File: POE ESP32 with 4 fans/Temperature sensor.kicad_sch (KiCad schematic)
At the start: 1 part, among them U1 DS18B20

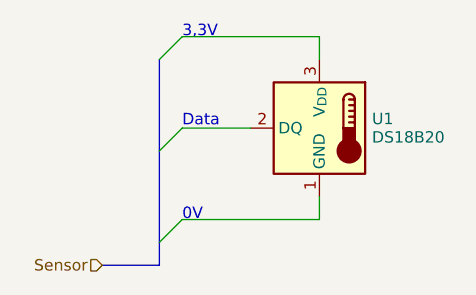
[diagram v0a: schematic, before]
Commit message: Assigned footprints to multiple symbols Removed automatic workflow triggering. Will change in the future
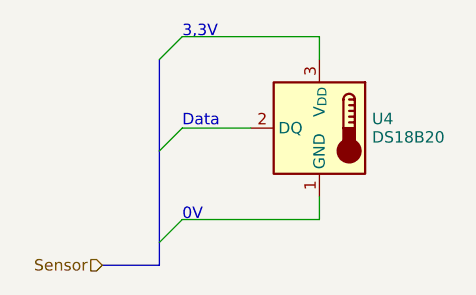
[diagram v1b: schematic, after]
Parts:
- U4: renamed from U1; footprint Package_TO_SOT_THT:TO-92_Inline -> (none)
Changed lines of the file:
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@@
 		(on_board yes)
 		(dnp no)
-		(property "Reference" "U1"
+		(property "Reference" "U4"
 			(at 68.0719 34.536 0)
 			(effects
@@
 			)
 		)
-		(property "Footprint" "Package_TO_SOT_THT:TO-92_Inline"
+		(property "Footprint" ""
 			(at 87.63 41.91 0)
 			(effects
